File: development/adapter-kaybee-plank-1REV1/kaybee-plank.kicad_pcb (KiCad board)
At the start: 2 copper layers, 39.5 x 51 mm, 27 parts, among them J1 Mini-DIN-6, J2 Conn_01x10, J3 Conn_01x10, J4 Mini-DIN-6, J5 USB_A, J7 TYPE-C-31-M-12, J8 Conn_01x02_Pin, J9 Conn_01x02_Pin, Q401 BCM857BS-7-F, Q402 BC2301T 2.8A, SW1 SW_SPDT

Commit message: kaybee production package
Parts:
- R408: value 66K -> 68K
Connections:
- SW1 pad : GND -> (no net)
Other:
- board text added: "PS/2 & USB Keyboard Sniffer Plank v1 REV1 feat. @therealDREG https://BusPirate.com"
- board text removed: "PS/2 & USB Keyboard Sniffer Plank REV0 feat. @therealDREG https://BusPirate.com"
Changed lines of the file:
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@@
 			(plot_on_all_layers_selection 0x00000000_00000000_00000000_00000000)
 			(disableapertmacros no)
-			(usegerberextensions no)
+			(usegerberextensions yes)
 			(usegerberattributes yes)
 			(usegerberadvancedattributes yes)
@@
 			(psa4output no)
 			(plot_black_and_white yes)
-			(plotinvisibletext no)
 			(sketchpadsonfab no)
 			(plotpadnumbers no)
@@
 			)
 		)
+		(property "szlcsc_partnum" "C21714127"
+			(at 0 0 180)
+			(unlocked yes)
+			(layer "F.Fab")
+			(hide yes)
+			(effects
+				(font
+					(size 1 1)
+					(thickness 0.15)
+				)
+			)
+		)
 		(property ki_fp_filters "SOT?23*")
 		(sheetname "/")
@@
 			)
 		)
+		(property "szlcsc_partnum" "C149504"
+			(at 0 0 270)
+			(unlocked yes)
+			(layer "F.Fab")
+			(hide yes)
+			(effects
+				(font
+					(size 1 1)
+					(thickness 0.15)
+				)
+			)
+		)
 		(property ki_fp_filters "R_*")
 		(sheetname "/")
@@
 			)
 		)
+		(property "szlcsc_partnum" "C105896"
+			(at 0 0 180)
+			(unlocked yes)
+			(layer "F.Fab")
+			(hide yes)
+			(effects
+				(font
+					(size 1 1)
+					(thickness 0.15)
+				)
+			)
+		)
 		(property ki_fp_filters "SC?70* SC?88* SOT?363* SOT?23*")
 		(sheetname "/")
@@
 			)
 		)
-		(property "Value" "66K"
+		(property "Value" "68K"
 			(at 0 1.65 90)
 			(layer "F.Fab")
@@
 			)
 		)
+		(property "szlcsc_partnum" "C17801"
+			(at 0 0 90)
+			(unlocked yes)
+			(layer "F.Fab")
+			(hide yes)
+			(effects
+				(font
+					(size 1 1)
+					(thickness 0.15)
+				)
+			)
+		)
 		(property ki_fp_filters "R_*")
 		(sheetname "/")
@@
 			)
 		)
+		(property "szlcsc_partnum" "C2828426"
+			(at 0 0 0)
+			(unlocked yes)
+			(layer "F.Fab")
+			(hide yes)
+			(effects
+				(font
+					(size 1 1)
+					(thickness 0.15)
+				)
+			)
+		)
 		(property ki_fp_filters "D*SOD?323*")
 		(sheetname "/")
@@
 			)
 		)
+		(property "szlcsc_partnum" "C17414"
+			(at 0 0 90)
+			(unlocked yes)
+			(layer "F.Fab")
+			(hide yes)
+			(effects
+				(font
+					(size 1 1)
+					(thickness 0.15)
+				)
+			)
+		)
 		(property ki_fp_filters "R_*")
 		(sheetname "/")
@@
 			(size 1 0.8)
 			(layers "F.Cu" "F.Mask" "F.Paste")
-			(net 11 "GND")
 		)
 		(pad "" smd rect
@@
 			(size 1 0.8)
 			(layers "F.Cu" "F.Mask" "F.Paste")
-			(net 11 "GND")
 		)
 		(pad "" np_thru_hole circle
@@
 			(size 1 0.8)
 			(layers "F.Cu" "F.Mask" "F.Paste")
-			(net 11 "GND")
 		)
 		(pad "" smd rect
@@
 			(size 1 0.8)
 			(layers "F.Cu" "F.Mask" "F.Paste")
-			(net 11 "GND")
 		)
 		(pad "1" smd rect
@@
 		)
 	)
-	(gr_text "PS/2 & USB Keyboard \nSniffer Plank REV0\nfeat. @therealDREG\nhttps://BusPirate.com"
+	(gr_text "PS/2 & USB Keyboard \nSniffer Plank v1 REV1\nfeat. @therealDREG\nhttps://BusPirate.com"
 		(at 120.777 97.536 90)
 		(layer "B.SilkS")
@@
 			(font
 				(size 1 1)
-				(thickness 0.15)
+				(thickness 0.2)
+				(bold yes)
 			)
 			(justify mirror)

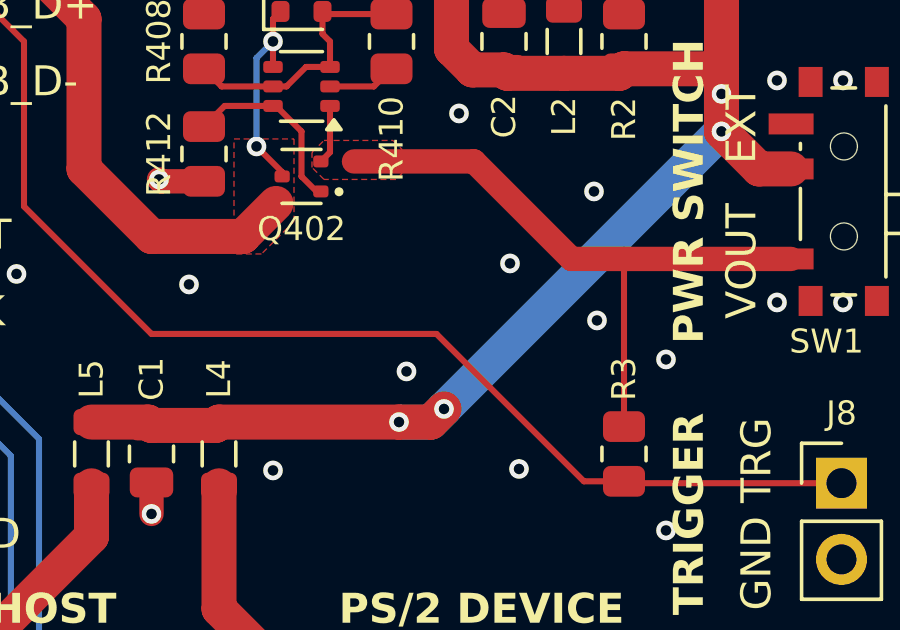
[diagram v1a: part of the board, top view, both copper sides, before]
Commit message: kaybee plank - change pull-up resistor supply source
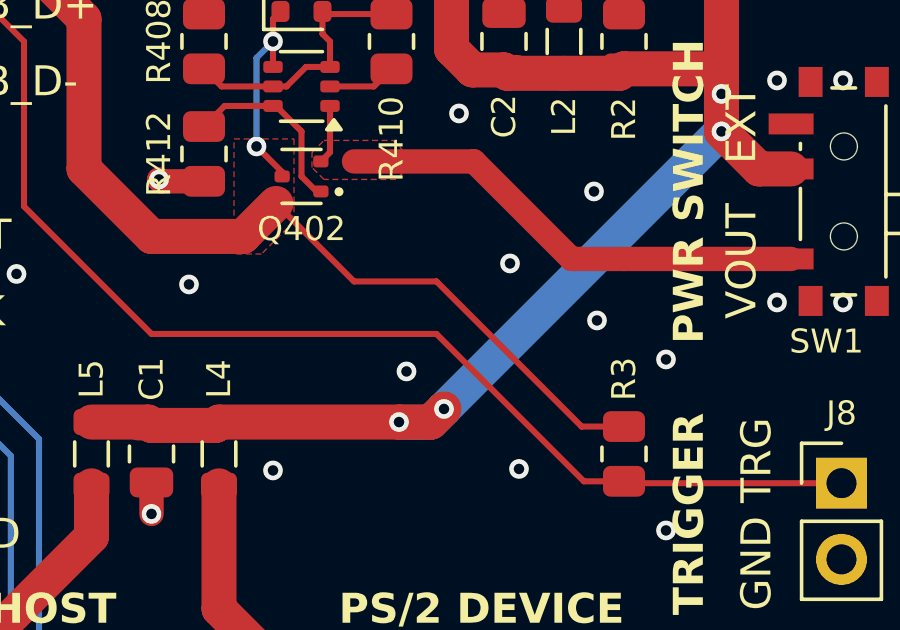
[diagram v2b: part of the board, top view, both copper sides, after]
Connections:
- R3 pad 2: VOUT -> VOUT_BP_SIDE
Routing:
- net VOUT_BP_SIDE: track 32.8 -> 47.1 mm
- net VOUT: track 23.5 -> 17.9 mm
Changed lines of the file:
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@@
 			(layers "F.Cu" "F.Mask" "F.Paste")
 			(roundrect_rratio 0.243902)
-			(net 12 "VOUT")
+			(net 27 "VOUT_BP_SIDE")
 			(pintype "passive")
 		)
@@
 	)
 	(segment
-		(start 130 105.3375)
-		(end 130 99.75)
-		(width 0.2032)
-		(layer "F.Cu")
-		(net 12)
-	)
-	(segment
 		(start 120.2 94.65)
 		(end 120.2 96.195)
@@
 	)
 	(segment
+		(start 128.5875 105.3375)
+		(end 129.6458 105.3375)
+		(width 0.2032)
+		(layer "F.Cu")
+		(net 27)
+	)
+	(segment
+		(start 121 100.5)
+		(end 123.75 100.5)
+		(width 0.2032)
+		(layer "F.Cu")
+		(net 27)
+	)
+	(segment
 		(start 118.3 93.35)
 		(end 118.3 92.5)
@@
 	)
 	(segment
+		(start 118.4 97.9)
+		(end 121 100.5)
+		(width 0.2032)
+		(layer "F.Cu")
+		(net 27)
+	)
+	(segment
 		(start 114.25 99)
 		(end 117.3 99)
@@
 		(layer "F.Cu")
 		(net 27)
+	)
+	(segment
+		(start 123.75 100.5)
+		(end 128.5875 105.3375)
+		(width 0.2032)
+		(layer "F.Cu")
+		(net 27)
